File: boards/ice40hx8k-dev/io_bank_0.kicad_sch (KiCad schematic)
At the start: 22 parts, among them U1 ICE40HX8K-CT256

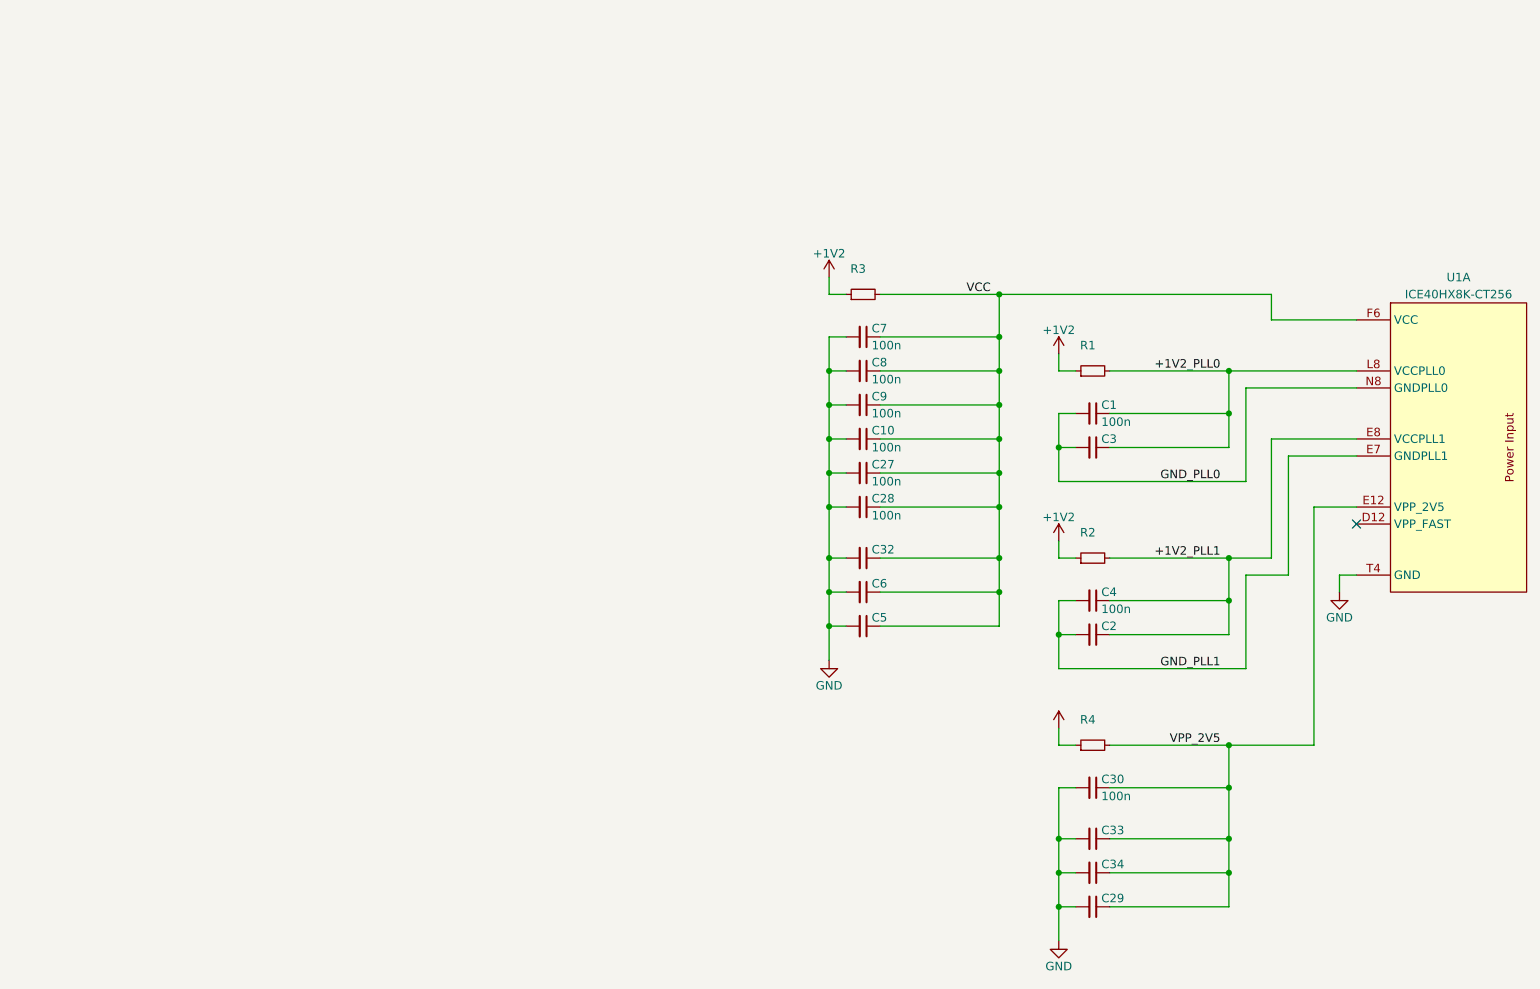
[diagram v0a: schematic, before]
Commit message: Split up schematic and label all nets.
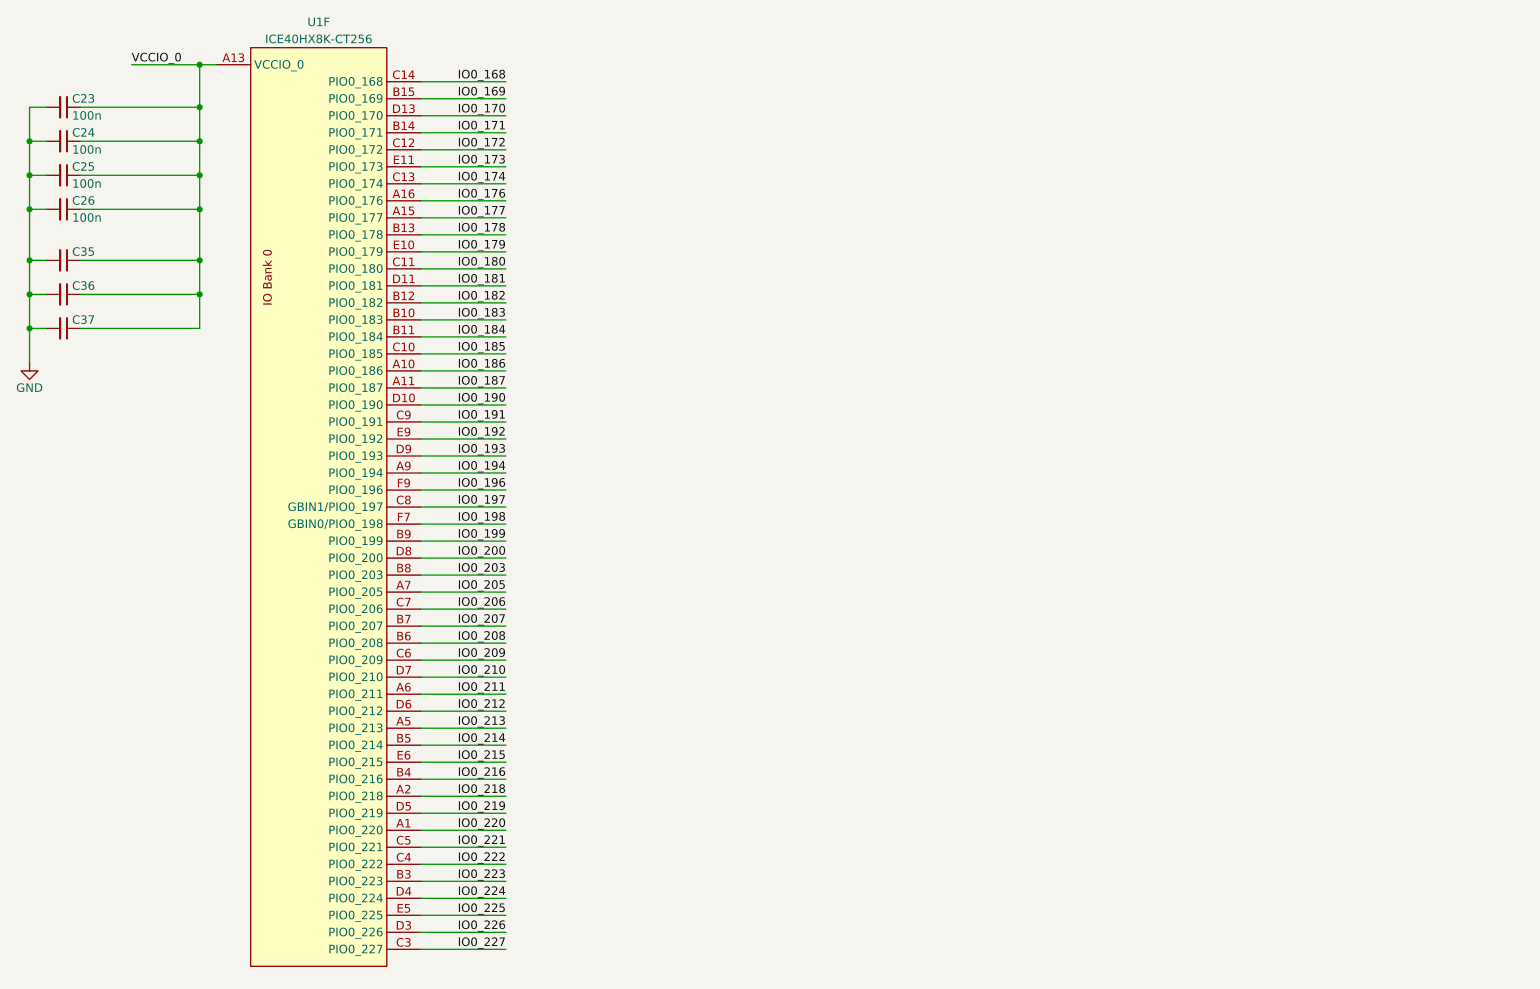
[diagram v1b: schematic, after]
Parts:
- removed C1, C10, C27, C28, C30, C4, C7, C8, C9: 100n, 0Local:C_SMD_0402_Pad0.5mm, symbol Device:C_Small
- removed C2, C29, C3, C32, C33, C34, C5, C6: (no value), 0Local:C_SMD_0402_Pad0.5mm, symbol Device:C_Small
- removed R1, R3: (no value), 0Local:R_SMD_0402_Pad0.5mm, symbol Device:R_Small
- removed R2, R4: (no value), symbol Device:R_Small
- removed U1: ICE40HX8K-CT256, 0Local:Lattice_caBGA-256_14x14mm_Layout16x16_P0.8mm_Ball0.4mm_Pad0.5mm_SMD, symbol 0Local:ICE40HX8K-CT256
- added C23, C24, C25, C26: 100n, 0Local:C_SMD_0402_Pad0.5mm, symbol Device:C_Small
- added C35, C36, C37: (no value), 0Local:C_SMD_0402_Pad0.5mm, symbol Device:C_Small
- added U1: ICE40HX8K-CT256, 0Local:Lattice_caBGA-256_14x14mm_Layout16x16_P0.8mm_Ball0.4mm_Pad0.5mm_SMD, symbol 0Local:ICE40HX8K-CT256
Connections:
- net GND: now also C23.2, C24.2, C25.2, C26.2, C35.2, C36.2, C37.2
- new net IO0_168: U1.C14 (PIO0_168)
- new net IO0_169: U1.B15 (PIO0_169)
- new net IO0_170: U1.D13 (PIO0_170)
- new net IO0_171: U1.B14 (PIO0_171)
- new net IO0_172: U1.C12 (PIO0_172)
- new net IO0_173: U1.E11 (PIO0_173)
- new net IO0_174: U1.C13 (PIO0_174)
- new net IO0_176: U1.A16 (PIO0_176)
- new net IO0_177: U1.A15 (PIO0_177)
- new net IO0_178: U1.B13 (PIO0_178)
- new net IO0_179: U1.E10 (PIO0_179)
- new net IO0_180: U1.C11 (PIO0_180)
- new net IO0_181: U1.D11 (PIO0_181)
- new net IO0_182: U1.B12 (PIO0_182)
- new net IO0_183: U1.B10 (PIO0_183)
- new net IO0_184: U1.B11 (PIO0_184)
- new net IO0_185: U1.C10 (PIO0_185)
- new net IO0_186: U1.A10 (PIO0_186)
- new net IO0_187: U1.A11 (PIO0_187)
- new net IO0_190: U1.D10 (PIO0_190)
- new net IO0_191: U1.C9 (PIO0_191)
- new net IO0_192: U1.E9 (PIO0_192)
- new net IO0_193: U1.D9 (PIO0_193)
- new net IO0_194: U1.A9 (PIO0_194)
- new net IO0_196: U1.F9 (PIO0_196)
- new net IO0_197: U1.C8 (GBIN1/PIO0_197)
- new net IO0_198: U1.F7 (GBIN0/PIO0_198)
- new net IO0_199: U1.B9 (PIO0_199)
- new net IO0_200: U1.D8 (PIO0_200)
- new net IO0_203: U1.B8 (PIO0_203)
- new net IO0_205: U1.A7 (PIO0_205)
- new net IO0_206: U1.C7 (PIO0_206)
- new net IO0_207: U1.B7 (PIO0_207)
- new net IO0_208: U1.B6 (PIO0_208)
- new net IO0_209: U1.C6 (PIO0_209)
- new net IO0_210: U1.D7 (PIO0_210)
- new net IO0_211: U1.A6 (PIO0_211)
- new net IO0_212: U1.D6 (PIO0_212)
- new net IO0_213: U1.A5 (PIO0_213)
- new net IO0_214: U1.B5 (PIO0_214)
- new net IO0_215: U1.E6 (PIO0_215)
- new net IO0_216: U1.B4 (PIO0_216)
- new net IO0_218: U1.A2 (PIO0_218)
- new net IO0_219: U1.D5 (PIO0_219)
- new net IO0_220: U1.A1 (PIO0_220)
- new net IO0_221: U1.C5 (PIO0_221)
- new net IO0_222: U1.C4 (PIO0_222)
- new net IO0_223: U1.B3 (PIO0_223)
- new net IO0_224: U1.D4 (PIO0_224)
- new net IO0_225: U1.E5 (PIO0_225)
- new net IO0_226: U1.D3 (PIO0_226)
- new net IO0_227: U1.C3 (PIO0_227)
- new net VCCIO_0: C23.1, C24.1, C25.1, C26.1, C35.1, C36.1, C37.1, U1.A13 (VCCIO_0), U1.A3 (VCCIO_0), U1.A8 (VCCIO_0), U1.F8 (VCCIO_0)
- no-connect marks 1 -> 0

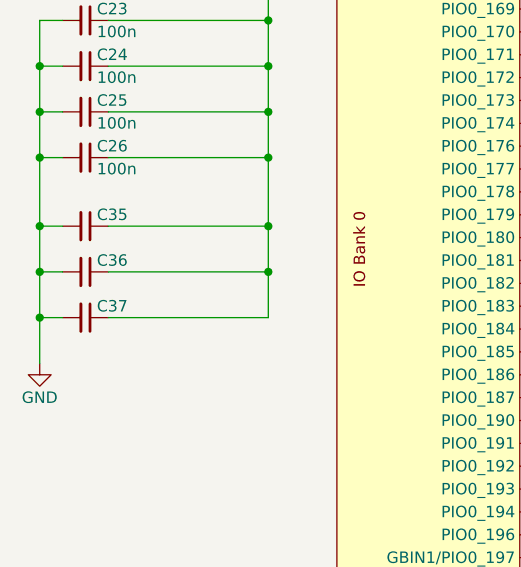
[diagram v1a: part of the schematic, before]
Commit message: Switch to 6 layers, add power fills under BGA.
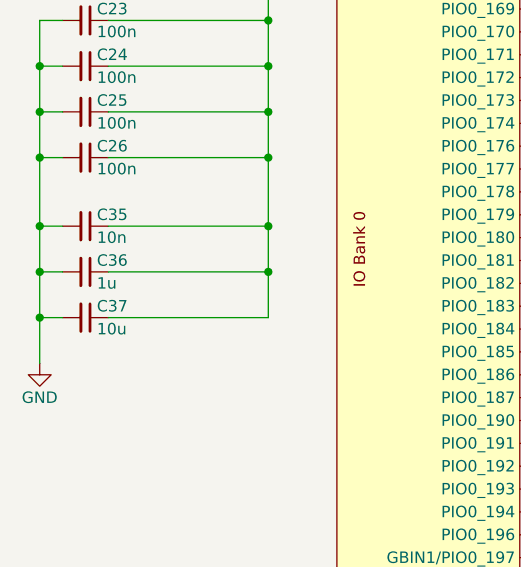
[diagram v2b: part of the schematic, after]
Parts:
- C35: value (none) -> 10n
- C36: value (none) -> 1u
- C37: value (none) -> 10u
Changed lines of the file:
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@@
       (effects (font (size 1.27 1.27)) (justify left))
     )
-    (property "Value" "" (id 1) (at 36.83 58.42 90)
+    (property "Value" "10n" (id 1) (at 36.83 58.42 90)
       (effects (font (size 1.27 1.27)) (justify left))
     )
@@
       (effects (font (size 1.27 1.27)) (justify left))
     )
-    (property "Value" "" (id 1) (at 36.83 63.5 90)
+    (property "Value" "1u" (id 1) (at 36.83 63.5 90)
       (effects (font (size 1.27 1.27)) (justify left))
     )
@@
       (effects (font (size 1.27 1.27)) (justify left))
     )
-    (property "Value" "" (id 1) (at 36.83 68.58 90)
-      (effects (font (size 1.27 1.27)) (justify left))
-    )
+    (property "Value" "10u" (id 1) (at 36.83 68.58 90)
+      (effects (font (size 1.27 1.27)) (justify left))
+    )

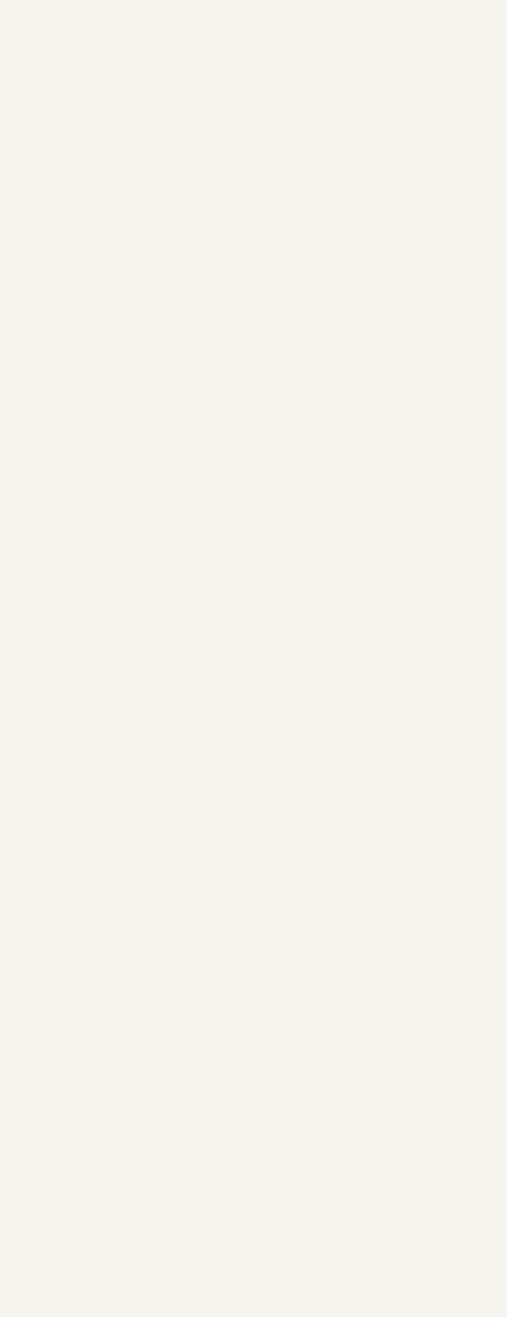
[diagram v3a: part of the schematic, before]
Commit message: Add Hirose connectors and standoffs.
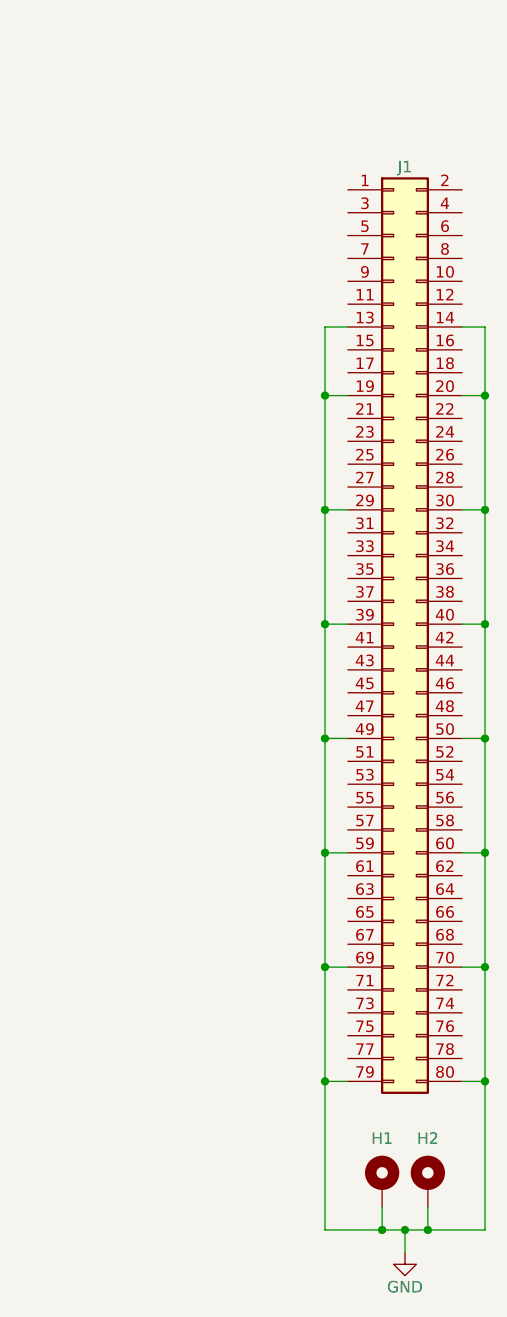
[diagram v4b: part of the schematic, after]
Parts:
- added H1, H2: 9774020633, Mounting_Wuerth:Mounting_Wuerth_WA-SMSI-M1.6_H2mm_9774020633, symbol Mechanical:MountingHole_Pad
- added J1: DF40HC(4.0)-80DS, 0Local:Hirose_DF40C-80DS, symbol Connector_Generic:Conn_02x40_Odd_Even
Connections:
- net GND: now also H1.1, H2.1, J1.13 (Pin_13), J1.14 (Pin_14), J1.19 (Pin_19), J1.20 (Pin_20), J1.29 (Pin_29), J1.30 (Pin_30), J1.39 (Pin_39), J1.40 (Pin_40), J1.49 (Pin_49), J1.50 (Pin_50), J1.59 (Pin_59), J1.60 (Pin_60), J1.69 (Pin_69), J1.70 (Pin_70), J1.79 (Pin_79), J1.80 (Pin_80)

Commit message: Switch to 4mm Hirose connectors and different mounting holes.
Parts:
- H1, H2: footprint Mounting_Wuerth:Mounting_Wuerth_WA-SMSI-M1.6_H2mm_9774020633 -> 0Local:MountingHole_2.2mm_M2_Pad6mm
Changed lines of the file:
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@@
       (effects (font (size 1.27 1.27)) hide)
     )
-    (property "Footprint" "Mounting_Wuerth:Mounting_Wuerth_WA-SMSI-M1.6_H2mm_9774020633" (id 2) (at 209.55 149.86 0)
+    (property "Footprint" "0Local:MountingHole_2.2mm_M2_Pad6mm" (id 2) (at 209.55 149.86 0)
       (effects (font (size 1.27 1.27)) hide)
     )
@@
       (effects (font (size 1.27 1.27)) hide)
     )
-    (property "Footprint" "Mounting_Wuerth:Mounting_Wuerth_WA-SMSI-M1.6_H2mm_9774020633" (id 2) (at 204.47 149.86 0)
+    (property "Footprint" "0Local:MountingHole_2.2mm_M2_Pad6mm" (id 2) (at 204.47 149.86 0)
       (effects (font (size 1.27 1.27)) hide)
     )
